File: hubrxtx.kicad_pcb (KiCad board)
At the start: 2 copper layers, 11.5 x 45 mm, 18 parts, among them J1 USB_B_Micro, U1 CH340K, U2 XC6206PxxxMR

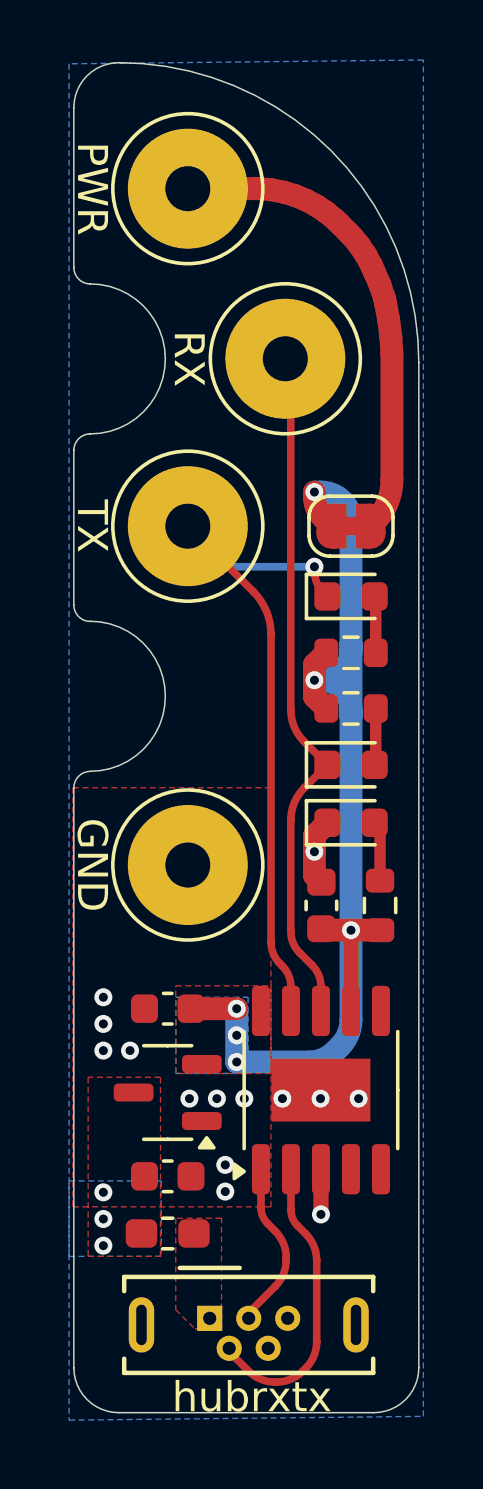
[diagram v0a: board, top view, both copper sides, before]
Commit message: Update KiCad project
* Cleanup schematic
* Add net classes
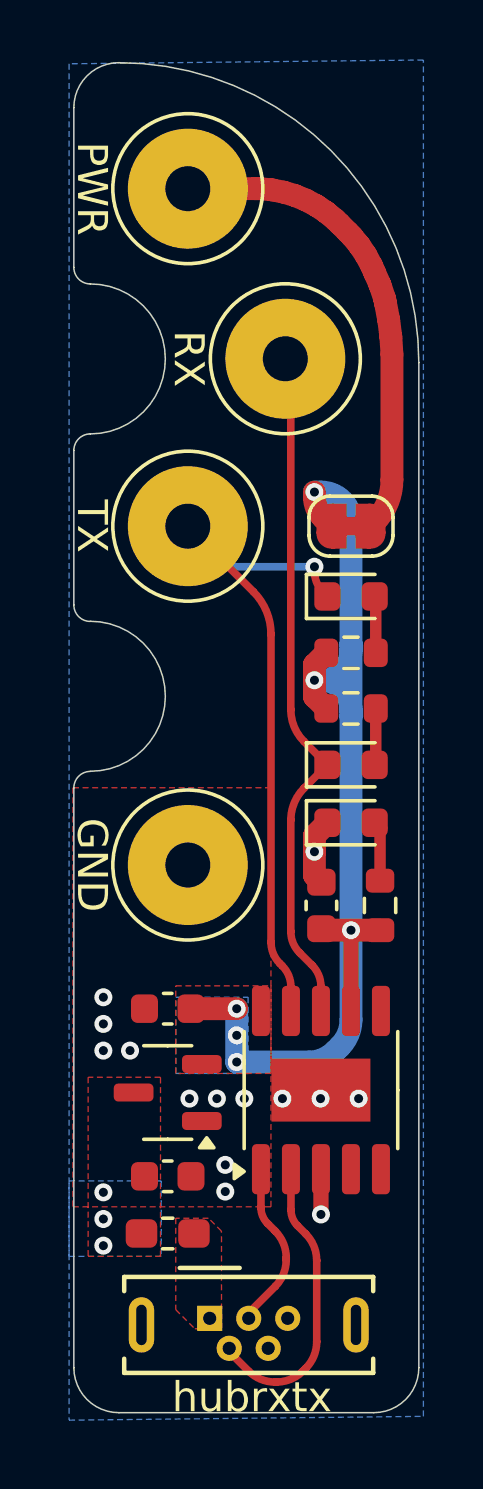
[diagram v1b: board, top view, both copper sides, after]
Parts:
- R1: value 470 -> 220Ω
- R2, R3: value 470 -> 22Ω
